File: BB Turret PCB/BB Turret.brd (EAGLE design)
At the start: 90.2 x 55.9 mm, 7 parts, among them M1 SERVO, M2 SERVO

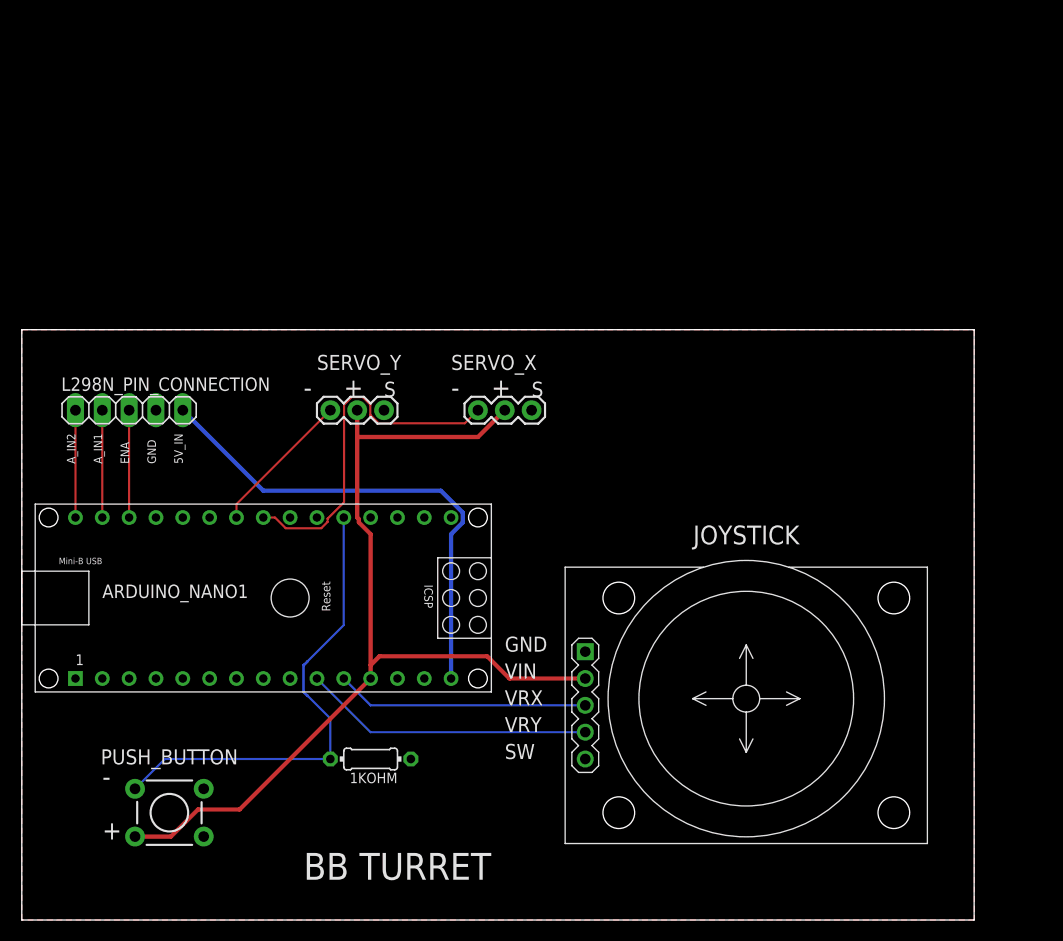
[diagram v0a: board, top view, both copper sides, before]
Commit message: Updated PCB files to be up to date with the code and current breadboard circuit. Updated images and README.
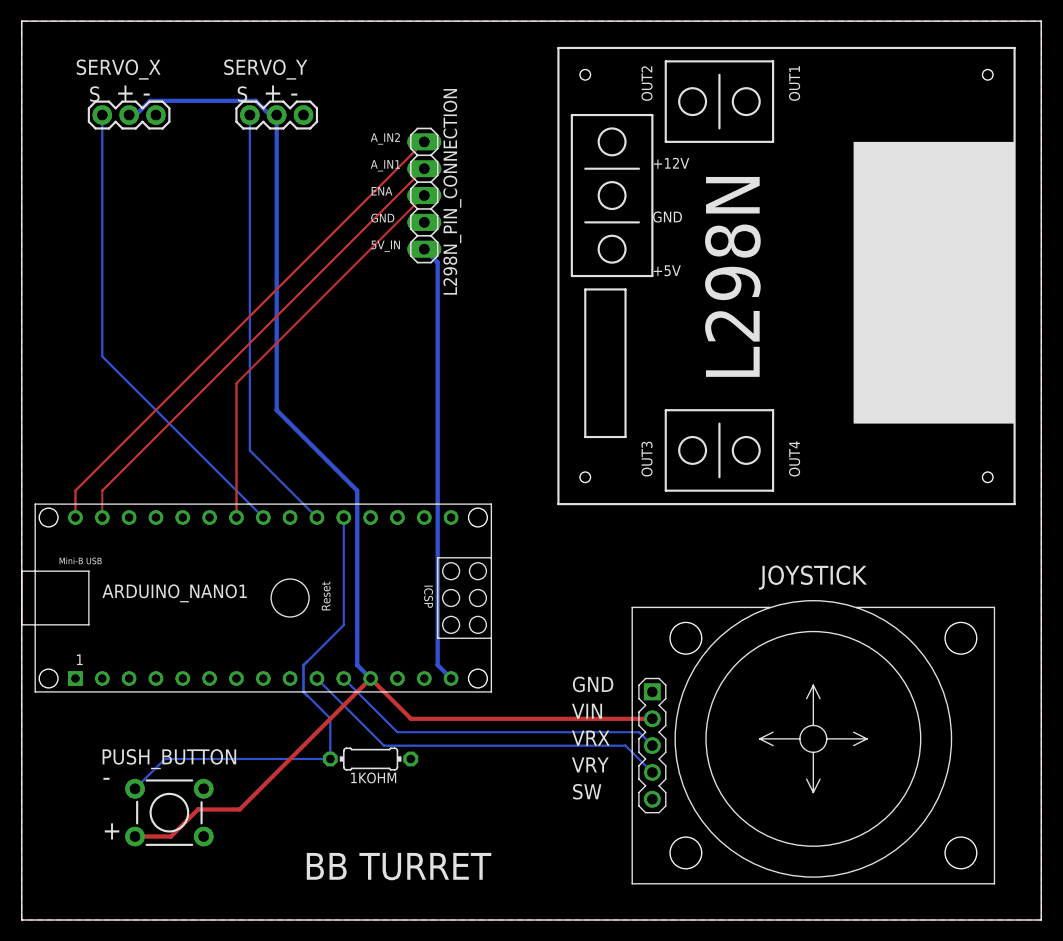
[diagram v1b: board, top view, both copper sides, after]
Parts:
- moved M1 45.2 mm to (7.62, 76.2)
- moved L298N_PIN_CONNECTION 34.5 mm to (38.1, 68.6), turned to 270 degrees
- moved M2 29.0 mm to (21.6, 76.2)
- moved JOYSTICK 7.41 mm to (74.9, 16.5)
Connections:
- net N$2 renamed A_IN2
- net N$3 renamed A_IN1
- net N$5 renamed 5V_IN
- removed net N$4: ARDUINO_NANO1.28, L298N_PIN_CONNECTION.3
- new net ENA: ARDUINO_NANO1.24, L298N_PIN_CONNECTION.3
- net SERVO_PWM2: now also ARDUINO_NANO1.21; no longer ARDUINO_NANO1.24
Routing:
- net A_IN2: track 10.2 -> 49.2 mm
- net 5V: track 91.0 -> 128.9 mm
- net ENA: track 0.00 -> 37.8 mm
- net A_IN1: track 10.2 -> 45.6 mm
- net SERVO_PWM2: track 13.8 -> 40.7 mm
- net SERVO_PWM1: track 33.6 -> 44.4 mm
- net N$4: track 10.2 -> 0.00 mm
- net VRY: track 27.5 -> 35.4 mm
- net VRX: track 23.9 -> 31.8 mm
- net 5V_IN: track 46.7 -> 41.7 mm
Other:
- board size 90.2 x 55.9 mm -> 96.5 x 85.1 mm
- board text added: "+12V"
- board text added: "+5V"
- board text added: "L298N"
- board text added: "OUT1"
- board text added: "OUT2"
- board text added: "OUT3"
- board text added: "OUT4"

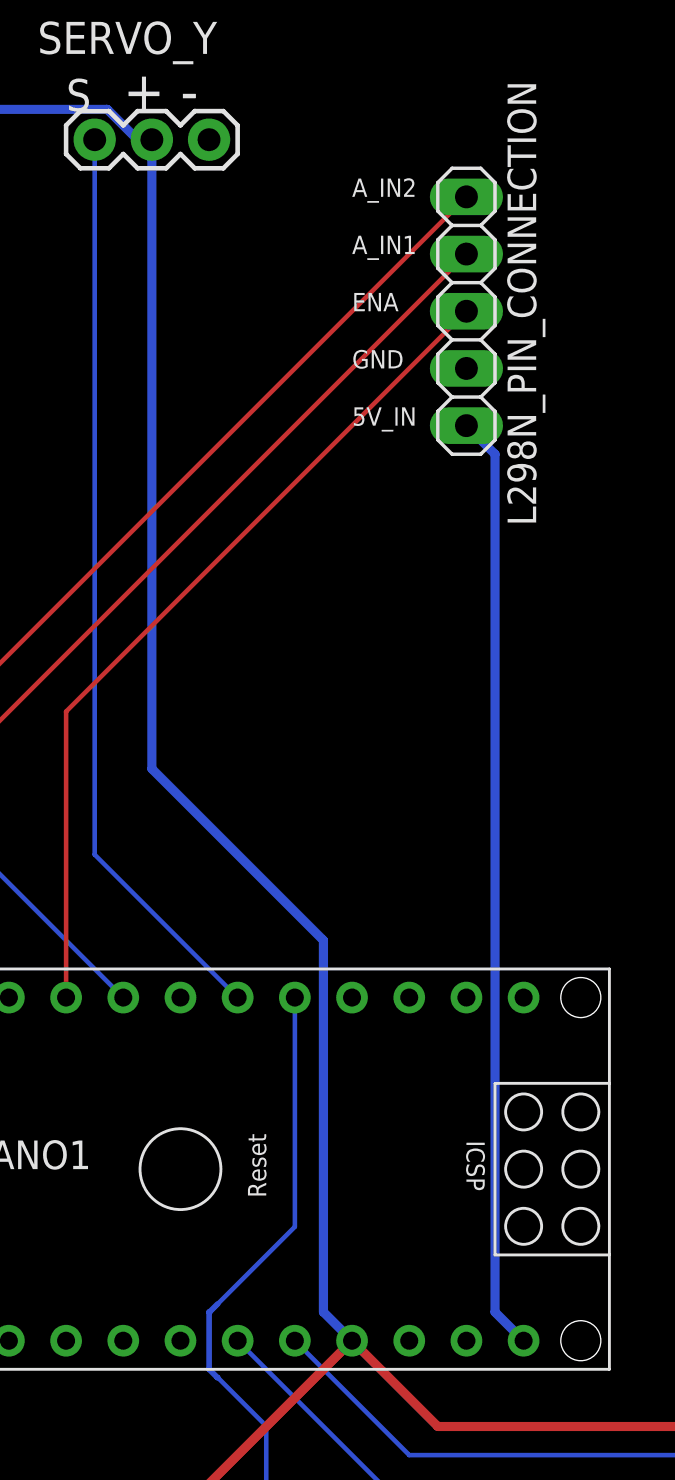
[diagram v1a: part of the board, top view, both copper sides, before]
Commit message: Fixed circuit and PCB so that the Arduino does not need USB power.
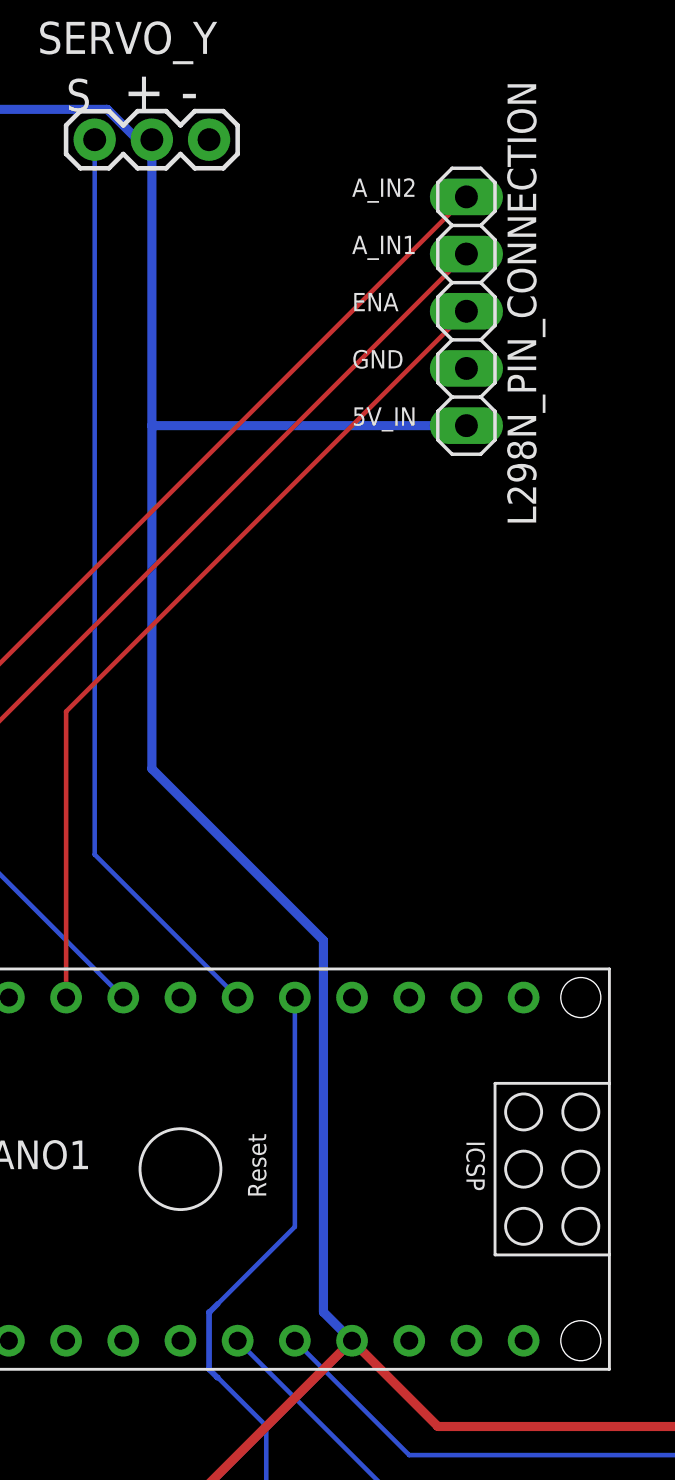
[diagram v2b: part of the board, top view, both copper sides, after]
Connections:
- removed net 5V_IN: ARDUINO_NANO1.15, L298N_PIN_CONNECTION.5
- new net VIN: ARDUINO_NANO1.15
- net 5V: now also L298N_PIN_CONNECTION.5
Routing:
- net 5V_IN: track 41.7 -> 0.00 mm
- net 5V: track 128.9 -> 142.8 mm
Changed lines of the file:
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@@
 <wire x1="27.0355875" y1="21.2244125" x2="27.0574" y2="21.2244125" width="0.254" layer="16"/>
-</signal>
-<signal name="5V">
-<contactref element="JOYSTICK" pad="2"/>
-<contactref element="PUSH_BUTTON" pad="3"/>
-<contactref element="M1" pad="2"/>
-<contactref element="M2" pad="2"/>
-<wire x1="14.119225" y1="7.8994" x2="10.7188" y2="7.8994" width="0.4064" layer="1"/>
-<wire x1="16.684625" y1="10.4648" x2="20.6248" y2="10.4648" width="0.4064" layer="1"/>
-<wire x1="16.684625" y1="10.4648" x2="14.119225" y2="7.8994" width="0.4064" layer="1"/>
-<contactref element="ARDUINO_NANO1" pad="12"/>
-<wire x1="20.6248" y1="10.4648" x2="33.02" y2="22.86" width="0.4064" layer="1"/>
-<wire x1="59.69" y1="19.05" x2="36.83" y2="19.05" width="0.4064" layer="1"/>
-<wire x1="33.02" y1="22.86" x2="36.83" y2="19.05" width="0.4064" layer="1"/>
-<wire x1="24.13" y1="76.2" x2="24.13" y2="48.26" width="0.4064" layer="16"/>
-<wire x1="24.13" y1="48.26" x2="31.75" y2="40.64" width="0.4064" layer="16"/>
-<wire x1="31.75" y1="40.64" x2="31.75" y2="24.13" width="0.4064" layer="16"/>
-<wire x1="31.75" y1="24.13" x2="33.02" y2="22.86" width="0.4064" layer="16"/>
-<wire x1="10.16" y1="76.2" x2="10.79618125" y2="76.2" width="0.4064" layer="16"/>
-<wire x1="23.49381875" y1="76.2" x2="24.13" y2="76.2" width="0.4064" layer="16"/>
-<wire x1="10.79618125" y1="76.2" x2="12.14238125" y2="77.5462" width="0.4064" layer="16"/>
-<wire x1="22.14761875" y1="77.5462" x2="23.49381875" y2="76.2" width="0.4064" layer="16"/>
-<wire x1="12.14238125" y1="77.5462" x2="22.14761875" y2="77.5462" width="0.4064" layer="16"/>
 </signal>
 <signal name="A_IN2">
@@
 <wire x1="7.62" y1="40.64" x2="7.62" y2="38.1" width="0.2032" layer="1"/>
 </signal>
-<signal name="5V_IN">
-<contactref element="L298N_PIN_CONNECTION" pad="5"/>
-<contactref element="ARDUINO_NANO1" pad="15"/>
-<wire x1="38.1" y1="63.5" x2="39.37" y2="62.23" width="0.4064" layer="16"/>
-<wire x1="39.37" y1="62.23" x2="39.37" y2="24.13" width="0.4064" layer="16"/>
-<wire x1="39.37" y1="24.13" x2="40.64" y2="22.86" width="0.4064" layer="16"/>
-</signal>
 <signal name="ENA">
 <contactref element="L298N_PIN_CONNECTION" pad="3"/>
@@
 <wire x1="20.32" y1="50.8" x2="20.32" y2="38.1" width="0.2032" layer="1"/>
 </signal>
+<signal name="VIN">
+<contactref element="ARDUINO_NANO1" pad="15"/>
+</signal>
+<signal name="5V">
+<contactref element="L298N_PIN_CONNECTION" pad="5"/>
+<contactref element="JOYSTICK" pad="2"/>
+<contactref element="PUSH_BUTTON" pad="3"/>
+<contactref element="M1" pad="2"/>
+<contactref element="M2" pad="2"/>
+<contactref element="ARDUINO_NANO1" pad="12"/>
+<wire x1="14.119225" y1="7.8994" x2="10.7188" y2="7.8994" width="0.4064" layer="1"/>
+<wire x1="16.684625" y1="10.4648" x2="20.6248" y2="10.4648" width="0.4064" layer="1"/>
+<wire x1="16.684625" y1="10.4648" x2="14.119225" y2="7.8994" width="0.4064" layer="1"/>
+<wire x1="20.6248" y1="10.4648" x2="33.02" y2="22.86" width="0.4064" layer="1"/>
+<wire x1="59.69" y1="19.05" x2="36.83" y2="19.05" width="0.4064" layer="1"/>
+<wire x1="33.02" y1="22.86" x2="36.83" y2="19.05" width="0.4064" layer="1"/>
+<wire x1="24.13" y1="76.2" x2="24.13" y2="63.5" width="0.4064" layer="16"/>
+<wire x1="24.13" y1="63.5" x2="24.13" y2="48.26" width="0.4064" layer="16"/>
+<wire x1="24.13" y1="48.26" x2="31.75" y2="40.64" width="0.4064" layer="16"/>
+<wire x1="31.75" y1="40.64" x2="31.75" y2="24.13" width="0.4064" layer="16"/>
+<wire x1="31.75" y1="24.13" x2="33.02" y2="22.86" width="0.4064" layer="16"/>
+<wire x1="10.16" y1="76.2" x2="10.79618125" y2="76.2" width="0.4064" layer="16"/>
+<wire x1="23.49381875" y1="76.2" x2="24.13" y2="76.2" width="0.4064" layer="16"/>
+<wire x1="10.79618125" y1="76.2" x2="12.14238125" y2="77.5462" width="0.4064" layer="16"/>
+<wire x1="22.14761875" y1="77.5462" x2="23.49381875" y2="76.2" width="0.4064" layer="16"/>
+<wire x1="12.14238125" y1="77.5462" x2="22.14761875" y2="77.5462" width="0.4064" layer="16"/>
+<wire x1="38.1" y1="63.5" x2="24.13" y2="63.5" width="0.4064" layer="16"/>
+</signal>
 </signals>
